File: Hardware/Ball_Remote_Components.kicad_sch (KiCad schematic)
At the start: 55 parts, among them J1 I2C_Gyro_Module, J2 USB_B_Micro, J3 SWD_Header, Q1 SI2333DS, SW1 SW_SPDT, U1 MCP73831-2-OT, U2 L3GD20, U3 STM32WB35, U4 LD3985M28R_SOT23, Y1 32MHz, Y2 32.768MHz

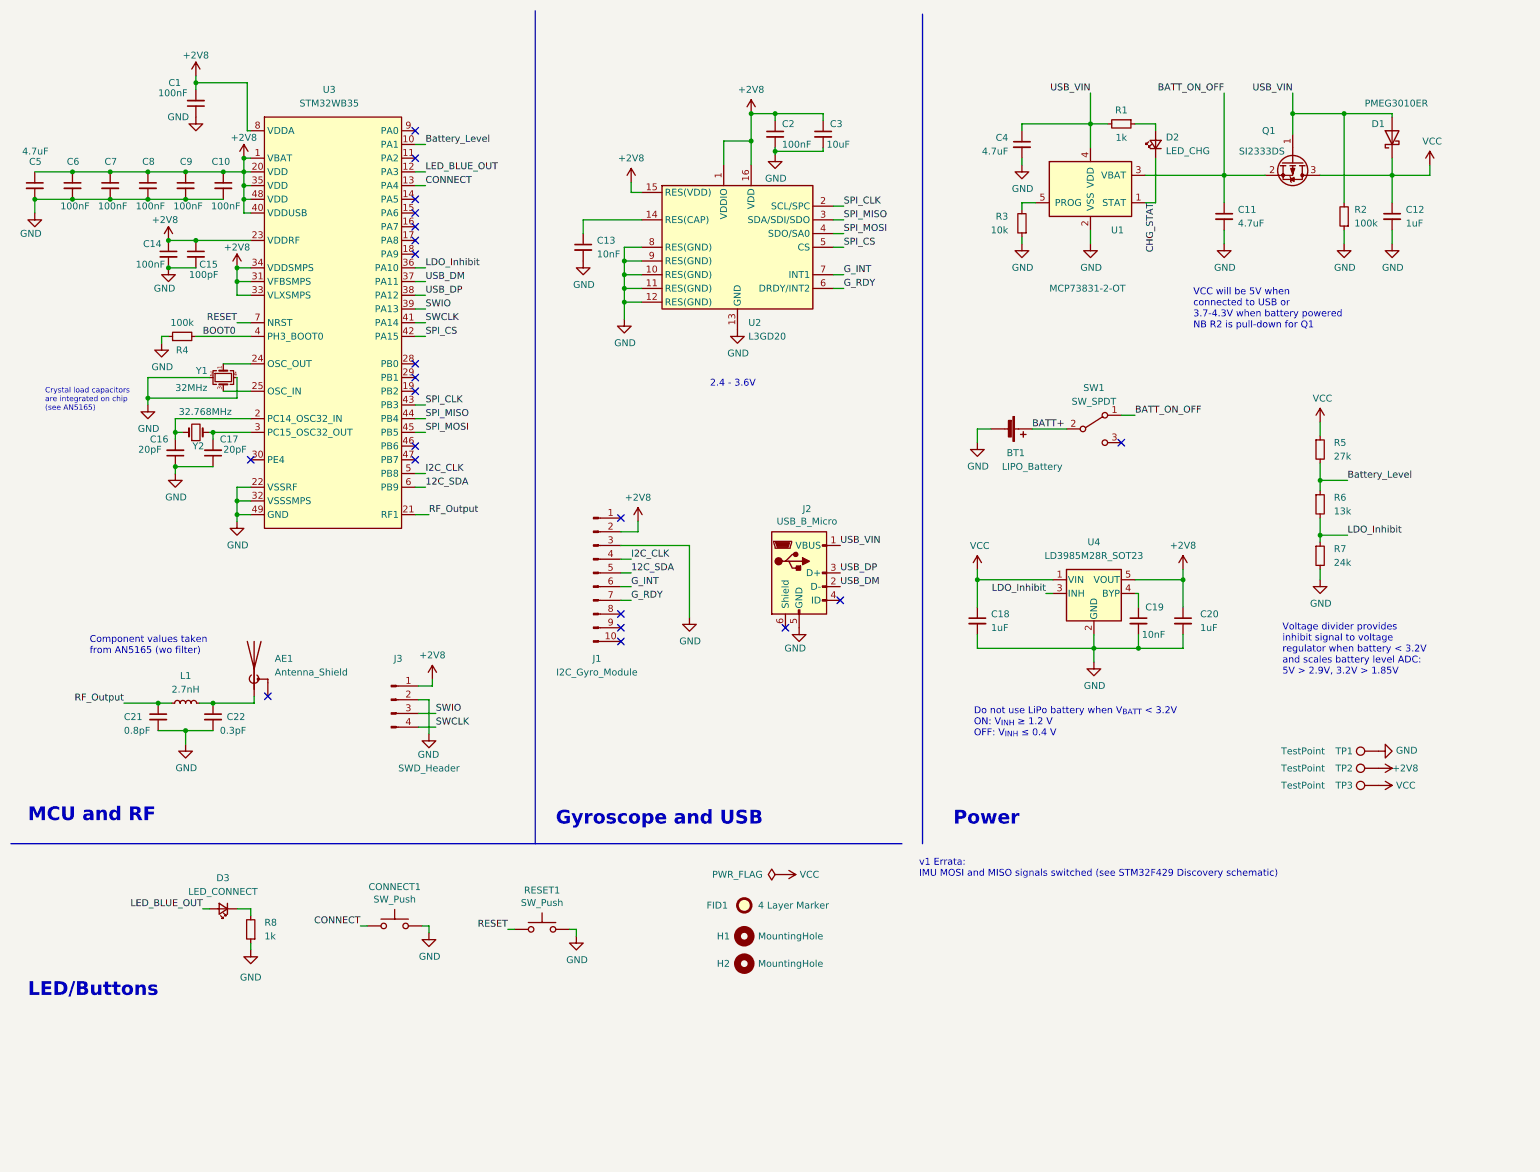
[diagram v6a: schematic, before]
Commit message: Cleaned up schematic to fix issues in Kicad 7; refactored USBClass to USBMain
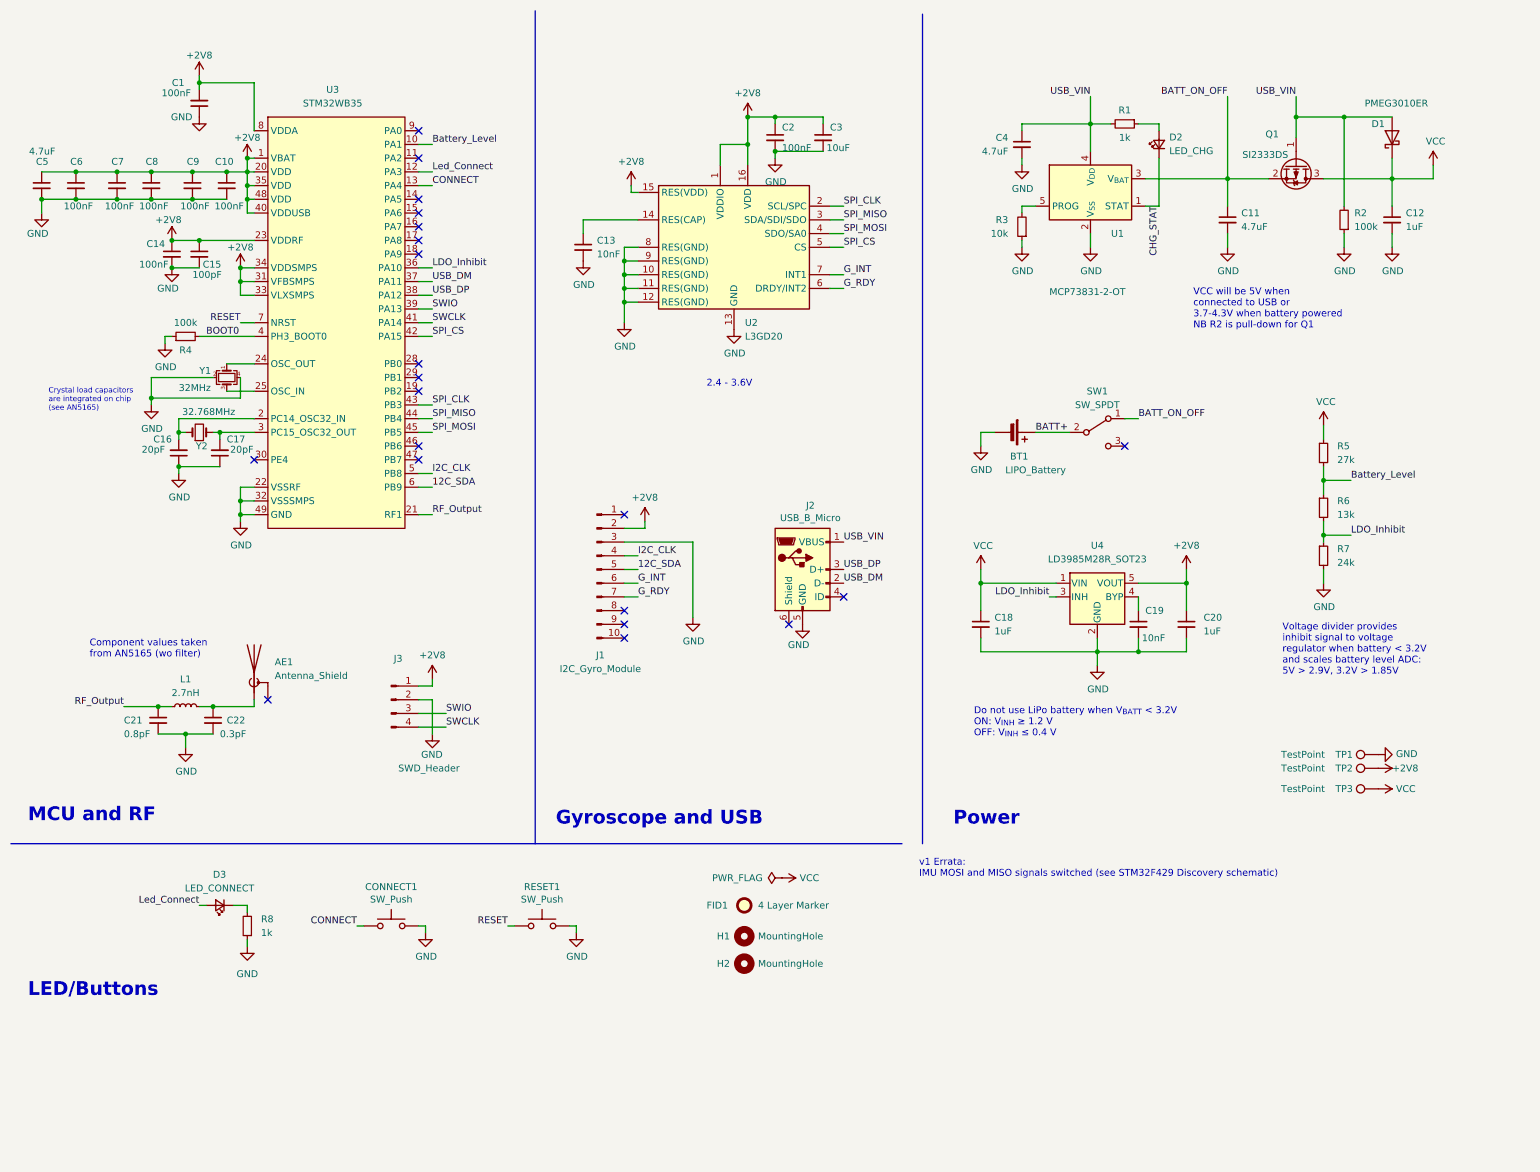
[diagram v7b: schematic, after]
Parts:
- J1: symbol Connector:Conn_01x10_Male -> Connector:Conn_01x10_Pin
- J3: symbol Connector:Conn_01x04_Male -> Connector:Conn_01x04_Pin
- U3: symbol STM32WB35:STM32WB35 -> STM32:STM32WB35
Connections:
- net LED_BLUE_OUT renamed Led_Connect
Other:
- moved on the sheet: AE1, BT1, C1, C10, C11, C12, C14, C15, C16, C17, C18, C19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

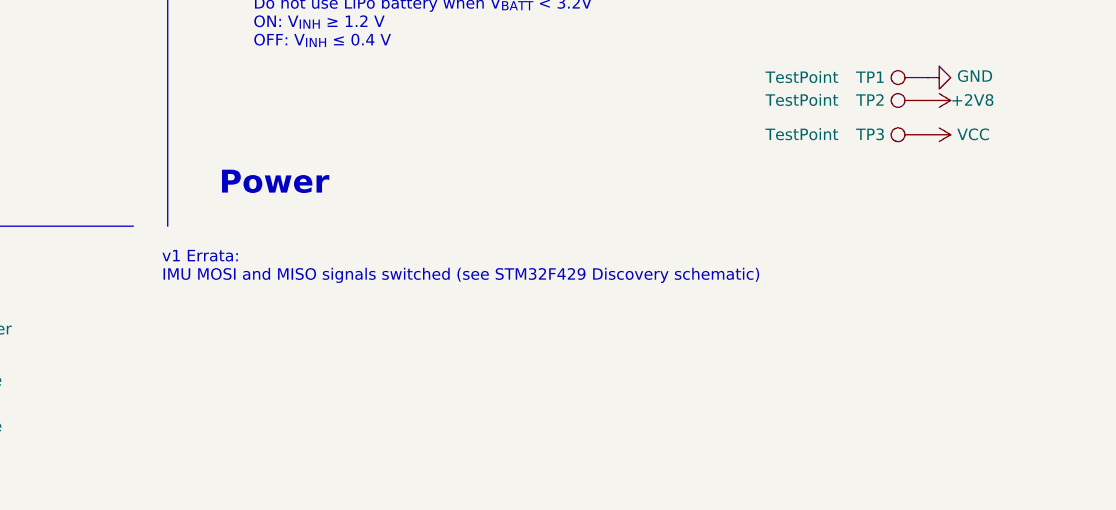
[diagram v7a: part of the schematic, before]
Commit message: Started configuring gyro ready to EXT interrupt
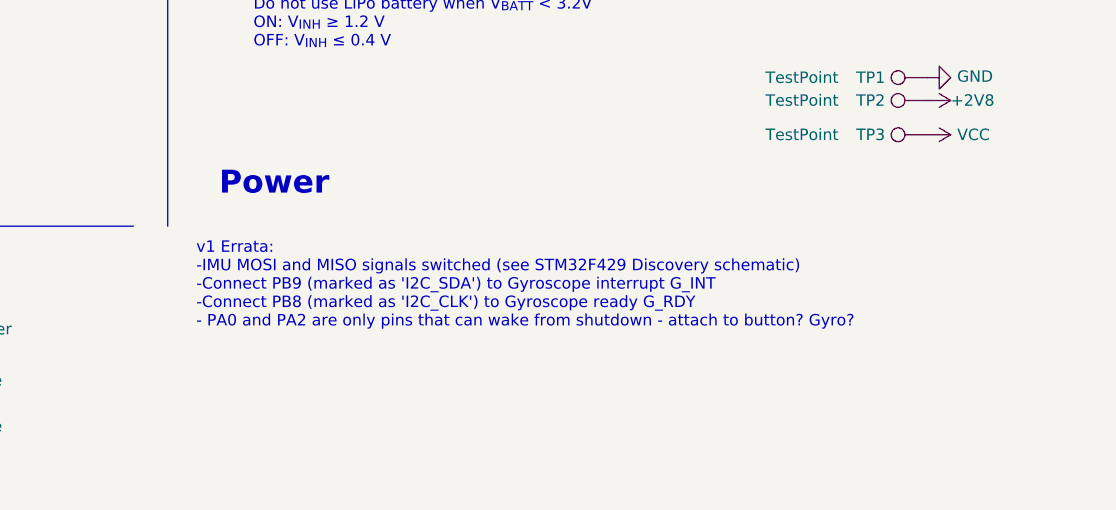
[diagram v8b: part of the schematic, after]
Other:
- note added: "v1 Errata: -IMU MOSI and MISO signals switched (see STM32F429 Discovery schematic) -Connect PB9 (marked as 'I2C_SDA') to Gyroscope interrupt G_INT -Connect PB8 (marked as 'I2C_CLK') to Gyroscope ready G_RDY - PA0 and PA2 are only pins that can wake from shutdown - attach to button? Gyro?"
- note removed: "v1 Errata: IMU MOSI and MISO signals switched (see STM32F429 Discovery schematic)"
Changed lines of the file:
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@@
     (effects (font (size 1.27 1.27)) (justify left bottom))
   )
-  (text "v1 Errata:\nIMU MOSI and MISO signals switched (see STM32F429 Discovery schematic)"
-    (at 180.34 172.72 0)
-    (effects (font (size 1.27 1.27)) (justify left bottom))
+  (text "v1 Errata:\n-IMU MOSI and MISO signals switched (see STM32F429 Discovery schematic)\n-Connect PB9 (marked as 'I2C_SDA') to Gyroscope interrupt G_INT\n-Connect PB8 (marked as 'I2C_CLK') to Gyroscope ready G_RDY\n- PA0 and PA2 are only pins that can wake from shutdown - attach to button? Gyro?\n"
+    (at 184.15 177.8 0)
+    (effects (font (size 1.27 1.27)) (justify left bottom) (href "#1"))
   )
   (text "Crystal load capacitors\nare integrated on chip\n(see AN5165)"
